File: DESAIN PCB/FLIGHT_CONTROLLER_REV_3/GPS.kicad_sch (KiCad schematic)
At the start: 17 parts, among them J10 GPS INPUT, J11 AVR-ISP-10, J9 FTDI BREAKOUT BOARD, SW2 SW_SPST, U3 ATmega328P-P, Y2 16 MHz

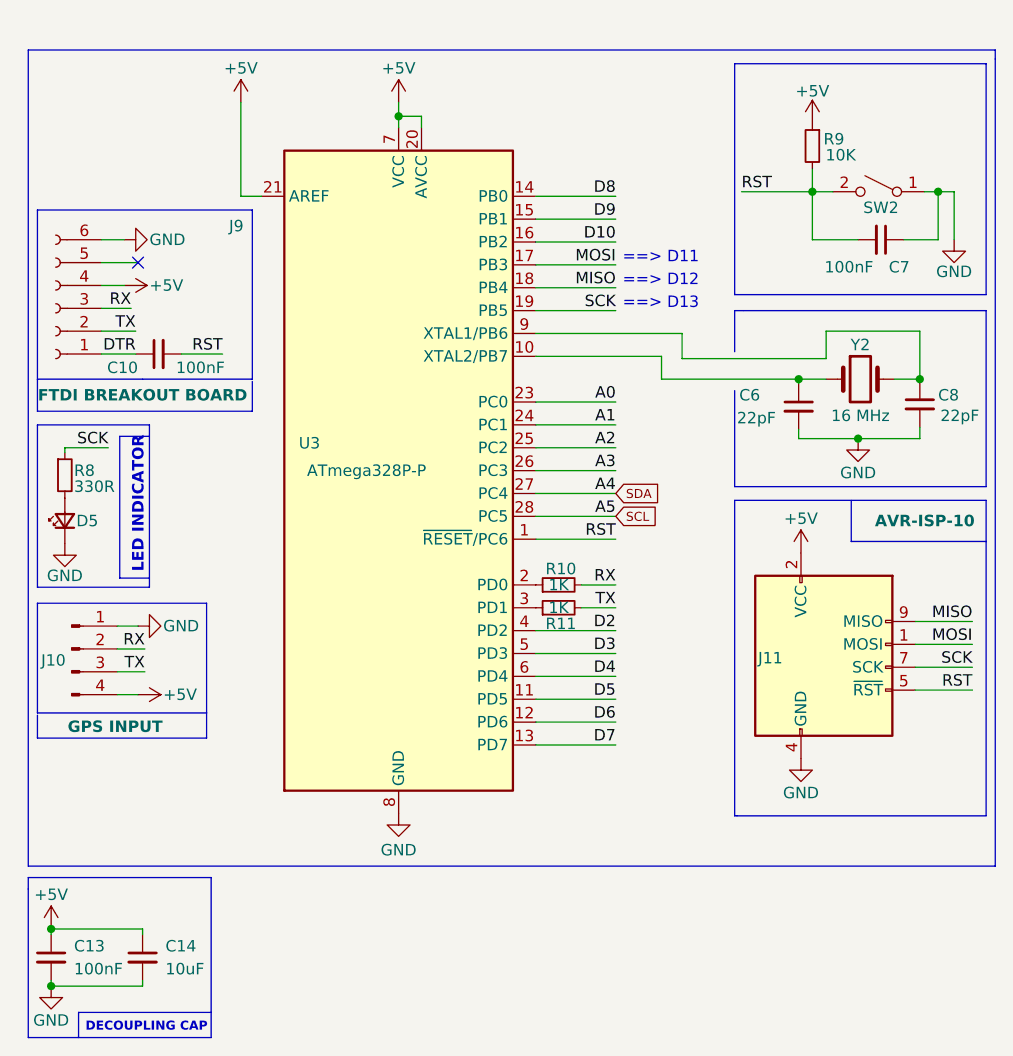
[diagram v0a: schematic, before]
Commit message: add new files
- more documentation files for PCB Rev 2
- add PCB Rev 3
- add 3D Models
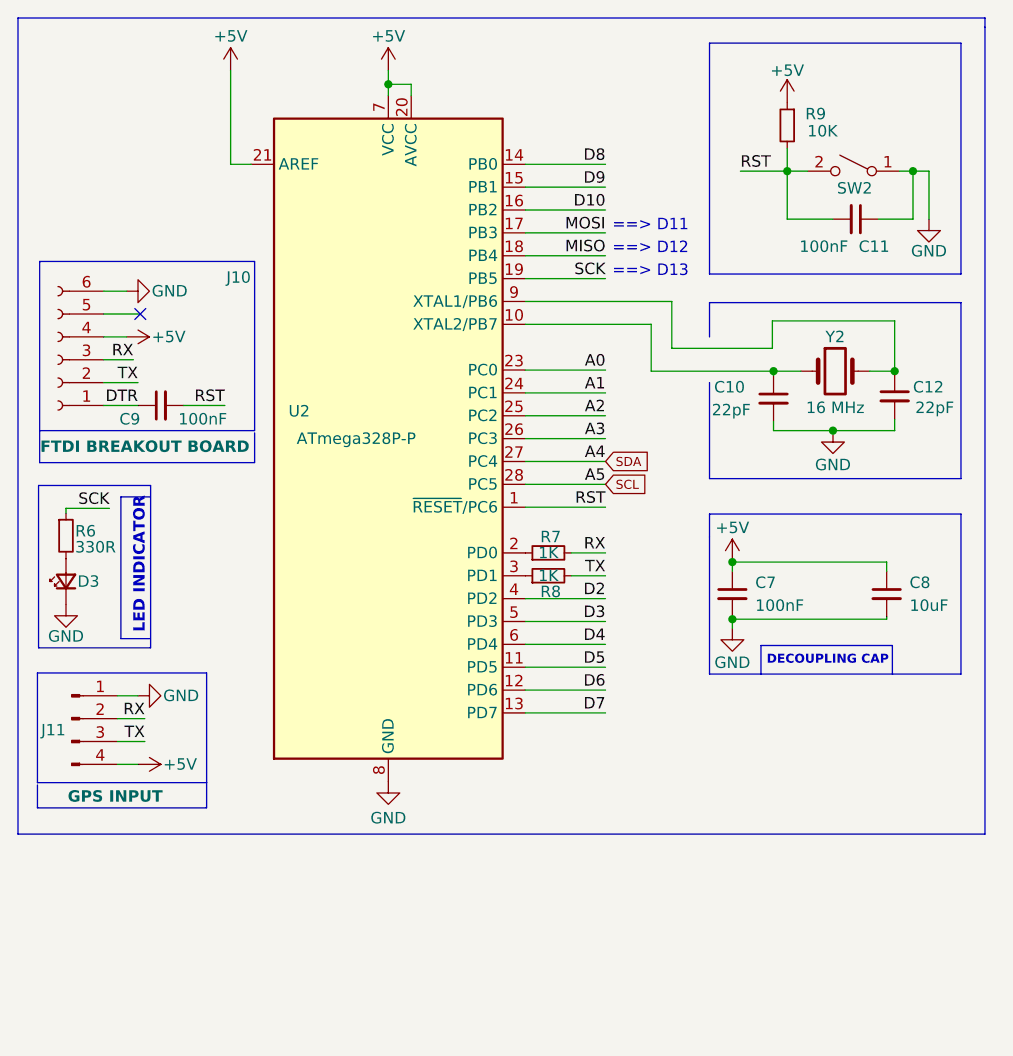
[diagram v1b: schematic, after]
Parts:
- removed C13: 100nF, Capacitor_THT:C_Disc_D5.0mm_W2.5mm_P2.50mm, symbol Device:C_Small
- removed C14: 10uF, Capacitor_THT:C_Disc_D5.0mm_W2.5mm_P2.50mm, symbol Device:C_Small
- removed C6: 22pF, Capacitor_THT:C_Disc_D5.0mm_W2.5mm_P2.50mm, symbol Device:C_Small
- removed D5: LED_Small, LED_THT:LED_D3.0mm, symbol Device:LED_Small
- removed J10: GPS INPUT, Connector_PinHeader_2.54mm:PinHeader_1x04_P2.54mm_Vertical, symbol Connector:Conn_01x04_Male
- removed J11: AVR-ISP-10, Connector_IDC:IDC-Header_2x05_P2.54mm_Vertical, symbol Connector:AVR-ISP-10
- removed J9: FTDI BREAKOUT BOARD, Connector_PinSocket_2.54mm:PinSocket_1x06_P2.54mm_Vertical, symbol Connector:Conn_01x06_Female
- removed R10, R11: 1K, Resistor_THT:R_Axial_DIN0207_L6.3mm_D2.5mm_P7.62mm_Horizontal, symbol Device:R_Small
- removed U3: ATmega328P-P, Package_DIP:DIP-28_W7.62mm, symbol MCU_Microchip_ATmega:ATmega328P-P
- added C11, C9: 100nF, Capacitor_SMD:C_0805_2012Metric_Pad1.18x1.45mm_HandSolder, symbol Device:C_Small
- added C12: 22pF, Capacitor_SMD:C_0805_2012Metric_Pad1.18x1.45mm_HandSolder, symbol Device:C_Small
- added D3: LED_Small, LED_THT:LED_D3.0mm, symbol Device:LED_Small
- added J10: FTDI BREAKOUT BOARD, Connector_PinSocket_2.54mm:PinSocket_1x06_P2.54mm_Vertical, symbol Connector:Conn_01x06_Female
- added J11: GPS INPUT, Connector_PinHeader_2.54mm:PinHeader_1x04_P2.54mm_Vertical, symbol Connector:Conn_01x04_Male
- added R6: 330R, Resistor_SMD:R_0805_2012Metric_Pad1.20x1.40mm_HandSolder, symbol Device:R_Small
- added R7: 1K, Resistor_SMD:R_0805_2012Metric_Pad1.20x1.40mm_HandSolder, symbol Device:R_Small
- added U2: ATmega328P-P, Package_DIP:DIP-28_W7.62mm, symbol MCU_Microchip_ATmega:ATmega328P-P
- C10: value 100nF -> 22pF; footprint Capacitor_THT:C_Disc_D5.0mm_W2.5mm_P2.50mm -> Capacitor_SMD:C_0805_2012Metric_Pad1.18x1.45mm_HandSolder
- C7: footprint Capacitor_THT:C_Disc_D5.0mm_W2.5mm_P2.50mm -> Capacitor_SMD:C_0805_2012Metric_Pad1.18x1.45mm_HandSolder
- C8: value 22pF -> 10uF; footprint Capacitor_THT:C_Disc_D5.0mm_W2.5mm_P2.50mm -> Capacitor_SMD:C_0805_2012Metric_Pad1.18x1.45mm_HandSolder
- R8: value 330R -> 1K; footprint Resistor_THT:R_Axial_DIN0207_L6.3mm_D2.5mm_P7.62mm_Horizontal -> Resistor_SMD:R_0805_2012Metric_Pad1.20x1.40mm_HandSolder
- R9: footprint Resistor_THT:R_Axial_DIN0207_L6.3mm_D2.5mm_P7.62mm_Horizontal -> Resistor_SMD:R_0805_2012Metric_Pad1.20x1.40mm_HandSolder
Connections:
- net +5V: now also C7.1, C8.1, J10.4 (Pin_4), J11.4 (Pin_4), U2.20 (AVCC), U2.21 (AREF), U2.7 (VCC)
- net A0: now also U2.23 (PC0)
- net A1: now also U2.24 (PC1)
- net A2: now also U2.25 (PC2)
- net A3: now also U2.26 (PC3)
- net D10: now also U2.16 (PB2)
- net D2: now also U2.4 (PD2)
- net D3: now also U2.5 (PD3)
- net D4: now also U2.6 (PD4)
- net D5: now also U2.11 (PD5)
- net D6: now also U2.12 (PD6)
- net D7: now also U2.13 (PD7)
- net D8: now also U2.14 (PB0)
- net D9: now also U2.15 (PB1)
- net DTR: now also C9.1, J10.1 (Pin_1); no longer C10.1
- net GND: now also C10.2, C7.2, C11.1, C12.2, D3.1 (K), J10.6 (Pin_6), J11.1 (Pin_1), U2.22 (GND), U2.8 (GND); no longer C7.1
- net MISO: now also U2.18 (PB4)
- net MOSI: now also U2.17 (PB3)
- net RST: now also C11.2, C9.2, U2.1 (~{RESET}/PC6); no longer C10.2, C7.2
- net RX: now also J10.3 (Pin_3), J11.2 (Pin_2), R7.2
- net SCK: now also R6.1, U2.19 (PB5); no longer R8.1
- net SCL: now also U2.28 (PC5)
- net SDA: now also U2.27 (PC4)
- net TX: now also R8.2, J10.2 (Pin_2), J11.3 (Pin_3)
- net at Y2.1: now also C10.1, U2.10 (XTAL2/PB7)
- net at Y2.2: now also C12.1, U2.9 (XTAL1/PB6); no longer C8.1
- new net: D3.2 (A), R6.2
- new net: R7.1, U2.2 (PD0)
- new net: R8.1, U2.3 (PD1)
